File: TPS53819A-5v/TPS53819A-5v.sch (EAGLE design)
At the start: 27 parts, among them IC1 TPS53819A

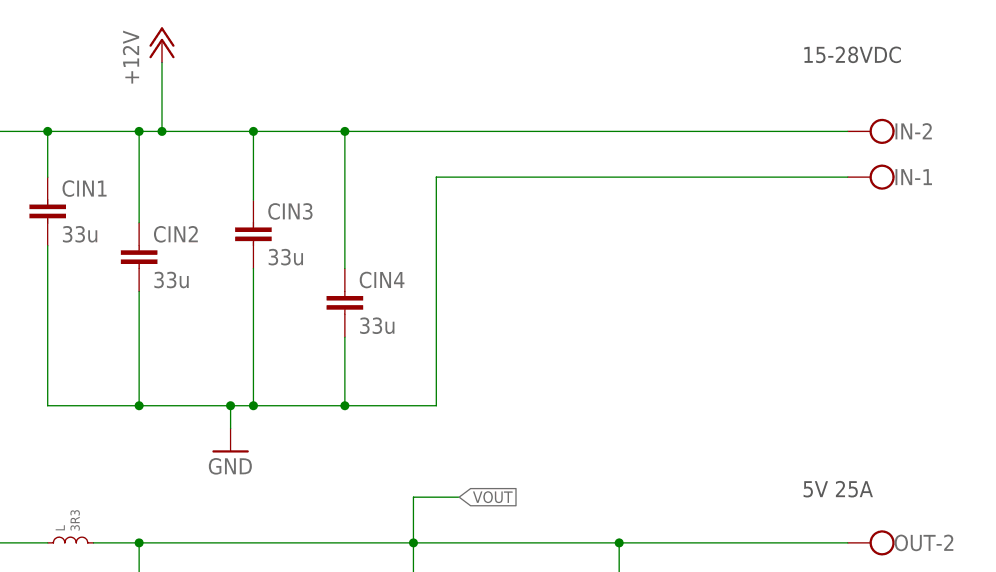
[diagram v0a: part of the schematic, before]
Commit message: made progress on routing, missing i2c connector still
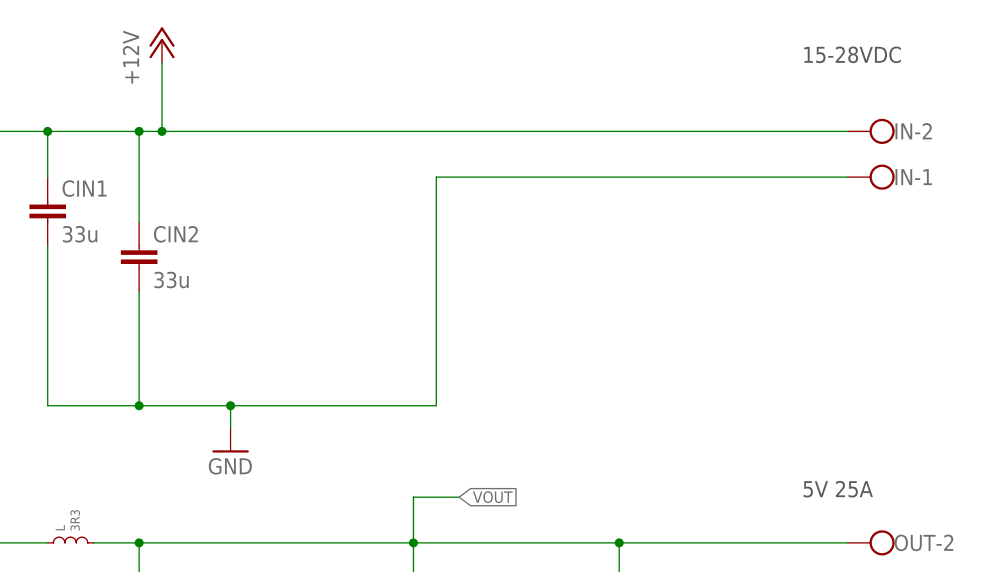
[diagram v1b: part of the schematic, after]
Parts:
- removed CIN3, CIN4: 33u, rcl:C-EUC2220K
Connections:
- net GND: no longer CIN3.2, CIN4.2
- net VDD: no longer CIN3.1, CIN4.1
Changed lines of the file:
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@@
 <grid distance="0.1" unitdist="inch" unit="inch" style="lines" multiple="1" display="no" altdistance="0.01" altunitdist="inch" altunit="inch"/>
 <layers>
-<layer number="1" name="Top" color="4" fill="1" visible="yes" active="no"/>
-<layer number="16" name="Bottom" color="1" fill="1" visible="yes" active="no"/>
-<layer number="17" name="Pads" color="2" fill="1" visible="yes" active="no"/>
-<layer number="18" name="Vias" color="2" fill="1" visible="yes" active="no"/>
-<layer number="19" name="Unrouted" color="14" fill="1" visible="yes" active="no"/>
-<layer number="20" name="Dimension" color="15" fill="1" visible="yes" active="no"/>
-<layer number="21" name="tPlace" color="7" fill="1" visible="yes" active="no"/>
-<layer number="22" name="bPlace" color="7" fill="1" visible="yes" active="no"/>
-<layer number="23" name="tOrigins" color="15" fill="1" visible="yes" active="no"/>
-<layer number="24" name="bOrigins" color="15" fill="1" visible="yes" active="no"/>
-<layer number="25" name="tNames" color="14" fill="1" visible="yes" active="no"/>
-<layer number="26" name="bNames" color="13" fill="1" visible="yes" active="no"/>
-<layer number="27" name="tValues" color="6" fill="1" visible="yes" active="no"/>
-<layer number="28" name="bValues" color="5" fill="1" visible="yes" active="no"/>
+<layer number="1" name="Top" color="4" fill="1" visible="no" active="no"/>
+<layer number="16" name="Bottom" color="1" fill="1" visible="no" active="no"/>
+<layer number="17" name="Pads" color="2" fill="1" visible="no" active="no"/>
+<layer number="18" name="Vias" color="2" fill="1" visible="no" active="no"/>
+<layer number="19" name="Unrouted" color="14" fill="1" visible="no" active="no"/>
+<layer number="20" name="Dimension" color="15" fill="1" visible="no" active="no"/>
+<layer number="21" name="tPlace" color="7" fill="1" visible="no" active="no"/>
+<layer number="22" name="bPlace" color="7" fill="1" visible="no" active="no"/>
+<layer number="23" name="tOrigins" color="15" fill="1" visible="no" active="no"/>
+<layer number="24" name="bOrigins" color="15" fill="1" visible="no" active="no"/>
+<layer number="25" name="tNames" color="14" fill="1" visible="no" active="no"/>
+<layer number="26" name="bNames" color="13" fill="1" visible="no" active="no"/>
+<layer number="27" name="tValues" color="6" fill="1" visible="no" active="no"/>
+<layer number="28" name="bValues" color="5" fill="1" visible="no" active="no"/>
 <layer number="29" name="tStop" color="7" fill="3" visible="no" active="no"/>
 <layer number="30" name="bStop" color="7" fill="6" visible="no" active="no"/>
@@
 <layer number="35" name="tGlue" color="7" fill="4" visible="no" active="no"/>
 <layer number="36" name="bGlue" color="7" fill="5" visible="no" active="no"/>
-<layer number="37" name="tTest" color="7" fill="1" visible="yes" active="no"/>
-<layer number="38" name="bTest" color="7" fill="1" visible="yes" active="no"/>
+<layer number="37" name="tTest" color="7" fill="1" visible="no" active="no"/>
+<layer number="38" name="bTest" color="7" fill="1" visible="no" active="no"/>
 <layer number="39" name="tKeepout" color="4" fill="11" visible="no" active="no"/>
 <layer number="40" name="bKeepout" color="1" fill="11" visible="no" active="no"/>
@@
 <layer number="44" name="Drills" color="7" fill="1" visible="no" active="no"/>
 <layer number="45" name="Holes" color="7" fill="1" visible="no" active="no"/>
-<layer number="46" name="Milling" color="3" fill="1" visible="yes" active="no"/>
-<layer number="47" name="Measures" color="7" fill="1" visible="yes" active="no"/>
-<layer number="48" name="Document" color="7" fill="1" visible="yes" active="no"/>
-<layer number="49" name="Reference" color="7" fill="1" visible="yes" active="no"/>
-<layer number="50" name="dxf" color="7" fill="1" visible="yes" active="no"/>
-<layer number="51" name="tDocu" color="7" fill="1" visible="yes" active="no"/>
-<layer number="52" name="bDocu" color="7" fill="1" visible="yes" active="no"/>
-<layer number="53" name="tGND_GNDA" color="7" fill="9" visible="yes" active="no"/>
-<layer number="54" name="bGND_GNDA" color="1" fill="9" visible="yes" active="no"/>
-<layer number="56" name="wert" color="7" fill="1" visible="yes" active="no"/>
-<layer number="57" name="tCAD" color="7" fill="1" visible="yes" active="no"/>
-<layer number="58" name="bCAD" color="7" fill="1" visible="yes" active="no"/>
-<layer number="59" name="tCarbon" color="7" fill="1" visible="yes" active="no"/>
-<layer number="60" name="bCarbon" color="7" fill="1" visible="yes" active="no"/>
+<layer number="46" name="Milling" color="3" fill="1" visible="no" active="no"/>
+<layer number="47" name="Measures" color="7" fill="1" visible="no" active="no"/>
+<layer number="48" name="Document" color="7" fill="1" visible="no" active="no"/>
+<layer number="49" name="Reference" color="7" fill="1" visible="no" active="no"/>
+<layer number="50" name="dxf" color="7" fill="1" visible="no" active="no"/>
+<layer number="51" name="tDocu" color="7" fill="1" visible="no" active="no"/>
+<layer number="52" name="bDocu" color="7" fill="1" visible="no" active="no"/>
+<layer number="53" name="tGND_GNDA" color="7" fill="9" visible="no" active="no"/>
+<layer number="54" name="bGND_GNDA" color="1" fill="9" visible="no" active="no"/>
+<layer number="56" name="wert" color="7" fill="1" visible="no" active="no"/>
+<layer number="57" name="tCAD" color="7" fill="1" visible="no" active="no"/>
+<layer number="58" name="bCAD" color="7" fill="1" visible="no" active="no"/>
+<layer number="59" name="tCarbon" color="7" fill="1" visible="no" active="no"/>
+<layer number="60" name="bCarbon" color="7" fill="1" visible="no" active="no"/>
 <layer number="88" name="SimResults" color="9" fill="1" visible="yes" active="yes"/>
 <layer number="89" name="SimProbes" color="9" fill="1" visible="yes" active="yes"/>
@@
 <part name="COUT4" library="rcl" deviceset="C-EU" device="C1206" value="22u"/>
 <part name="GND5" library="supply1" deviceset="GND" device=""/>
-<part name="CIN3" library="rcl" deviceset="C-EU" device="C2220K" value="33u"/>
-<part name="CIN4" library="rcl" deviceset="C-EU" device="C2220K" value="33u"/>
 <part name="IC1" library="TPS53819A" deviceset="TPS53819A" device=""/>
 <part name="GND2" library="supply1" deviceset="GND" device=""/>
@@
 <instance part="COUT4" gate="G$1" x="213.36" y="104.14"/>
 <instance part="GND5" gate="1" x="220.98" y="73.66"/>
-<instance part="CIN3" gate="G$1" x="190.5" y="167.64"/>
-<instance part="CIN4" gate="G$1" x="200.66" y="160.02"/>
 <instance part="IC1" gate="IC1" x="73.66" y="121.92"/>
 <instance part="GND2" gate="1" x="73.66" y="71.12"/>
@@
 <wire x1="256.54" y1="172.72" x2="210.82" y2="172.72" width="0.1524" layer="91"/>
 <wire x1="210.82" y1="172.72" x2="210.82" y2="147.32" width="0.1524" layer="91"/>
-<wire x1="210.82" y1="147.32" x2="200.66" y2="147.32" width="0.1524" layer="91"/>
 <junction x="187.96" y="147.32"/>
 <pinref part="CIN1" gate="G$1" pin="2"/>
 <pinref part="CIN2" gate="G$1" pin="2"/>
 <pinref part="GND3" gate="1" pin="GND"/>
-<wire x1="200.66" y1="147.32" x2="190.5" y2="147.32" width="0.1524" layer="91"/>
-<wire x1="190.5" y1="147.32" x2="187.96" y2="147.32" width="0.1524" layer="91"/>
+<wire x1="210.82" y1="147.32" x2="187.96" y2="147.32" width="0.1524" layer="91"/>
 <wire x1="187.96" y1="144.78" x2="187.96" y2="147.32" width="0.1524" layer="91"/>
-<wire x1="190.5" y1="162.56" x2="190.5" y2="147.32" width="0.1524" layer="91"/>
-<junction x="190.5" y="147.32"/>
-<wire x1="200.66" y1="154.94" x2="200.66" y2="147.32" width="0.1524" layer="91"/>
-<junction x="200.66" y="147.32"/>
-<pinref part="CIN3" gate="G$1" pin="2"/>
-<pinref part="CIN4" gate="G$1" pin="2"/>
 <pinref part="IN" gate="-1" pin="KL"/>
 </segment>
@@
 <junction x="177.8" y="177.8"/>
 <junction x="180.34" y="177.8"/>
-<wire x1="256.54" y1="177.8" x2="200.66" y2="177.8" width="0.1524" layer="91"/>
+<wire x1="256.54" y1="177.8" x2="180.34" y2="177.8" width="0.1524" layer="91"/>
 <pinref part="CIN1" gate="G$1" pin="1"/>
 <pinref part="CIN2" gate="G$1" pin="1"/>
 <pinref part="HS" gate="G$1" pin="D"/>
-<wire x1="200.66" y1="177.8" x2="190.5" y2="177.8" width="0.1524" layer="91"/>
-<wire x1="190.5" y1="177.8" x2="180.34" y2="177.8" width="0.1524" layer="91"/>
-<wire x1="190.5" y1="170.18" x2="190.5" y2="177.8" width="0.1524" layer="91"/>
-<junction x="190.5" y="177.8"/>
-<wire x1="200.66" y1="162.56" x2="200.66" y2="177.8" width="0.1524" layer="91"/>
-<junction x="200.66" y="177.8"/>
-<pinref part="CIN3" gate="G$1" pin="1"/>
-<pinref part="CIN4" gate="G$1" pin="1"/>
 <pinref part="CS" gate="G$1" pin="1"/>
 <wire x1="132.08" y1="165.1" x2="132.08" y2="167.64" width="0.1524" layer="91"/>
